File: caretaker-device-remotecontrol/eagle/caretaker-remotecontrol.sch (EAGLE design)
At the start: 50 parts, among them IC1 MAX1811N, IC2 ATMEGA168, IC3 XBee Series 2, IC4 ZLDO330, K1 BAT, K2 ISP, K3 USB-MINIB-5PIN, Q1 16MHz

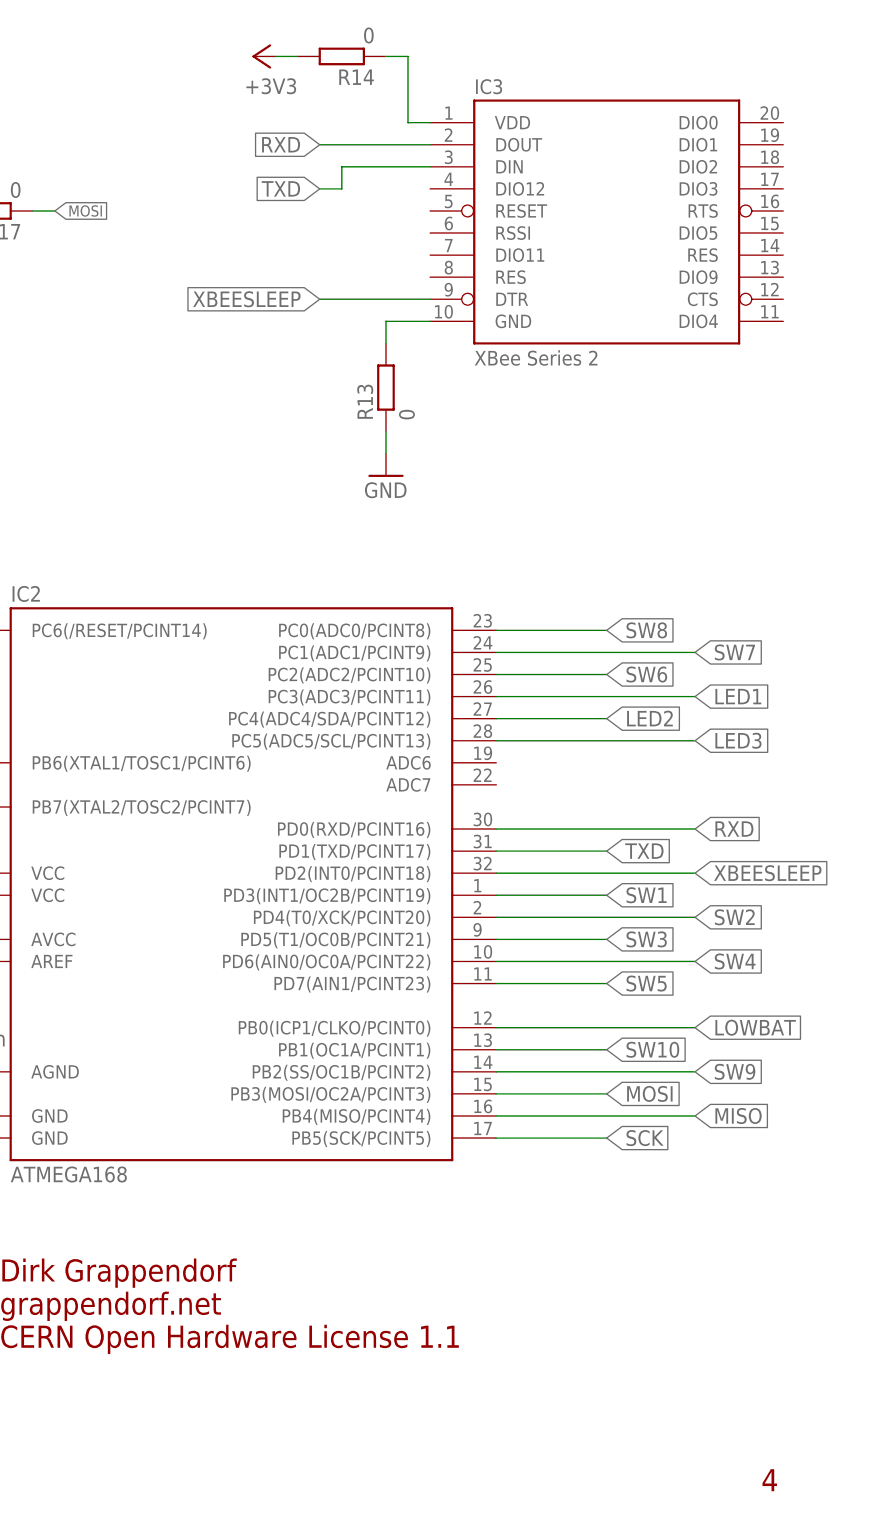
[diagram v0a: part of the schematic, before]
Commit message: feat: Convert the XBee RemoteControl device to a WLAN device
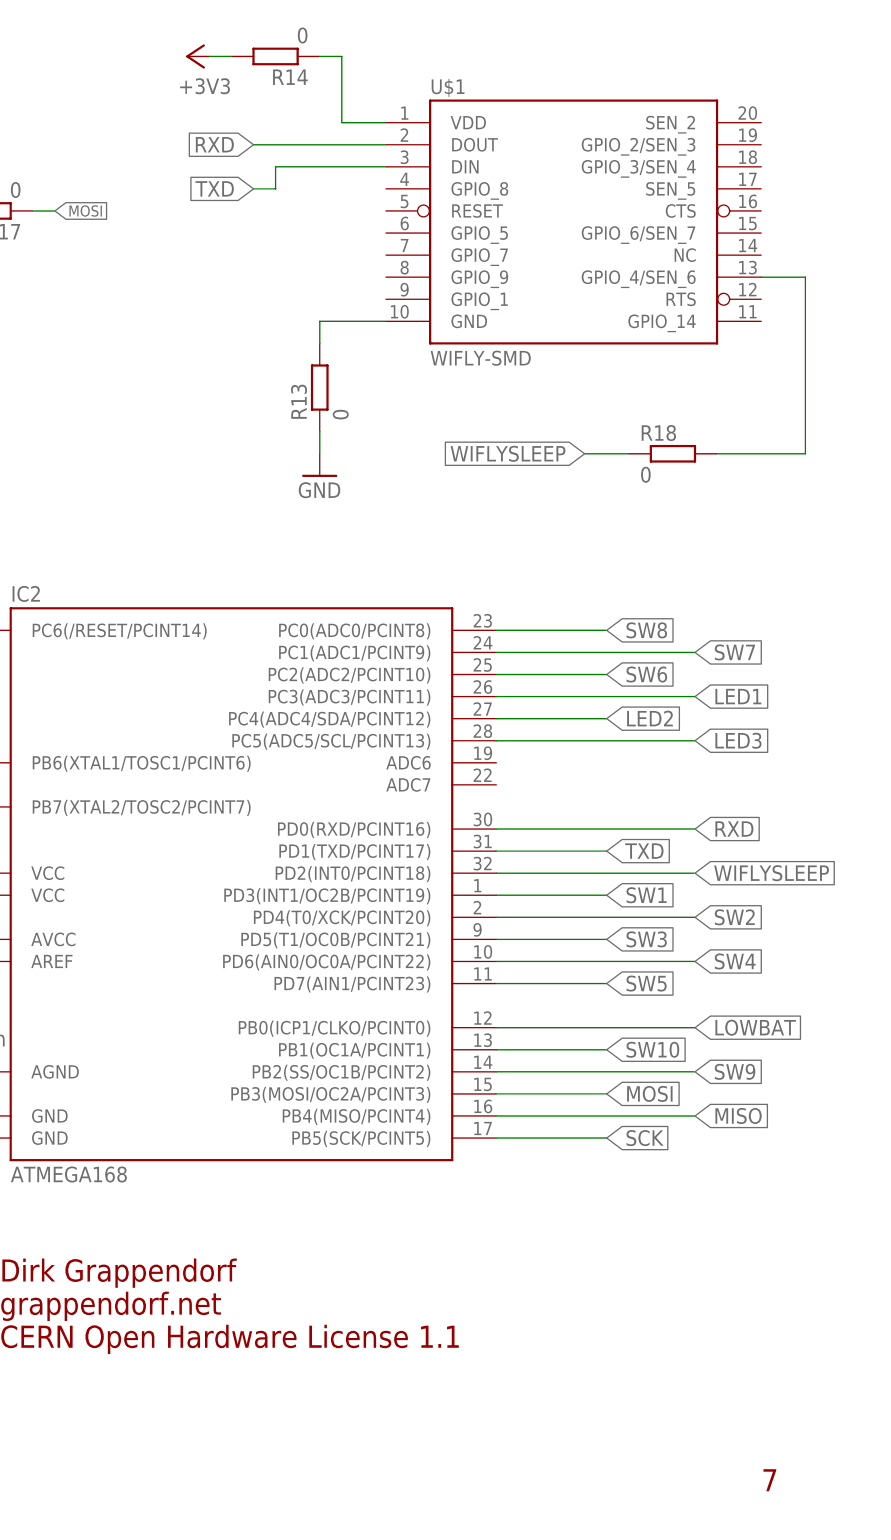
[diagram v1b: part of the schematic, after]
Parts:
- removed IC3: XBee Series 2, grapelabs:XBEE-1B4
- added R18: 0, rcl:R-EU_R1206
- added U$1: WIFLY-SMD, grapelabs:WIFLY-SMD
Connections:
- removed net XBEESLEEP: IC2.PD2(INT0/PCINT18), IC3.DTR
- new net N$27: R18.2, U$1.GPIO_4/SEN_6
- new net WIFLYSLEEP: IC2.PD2(INT0/PCINT18), R18.1
- net N$22: now also U$1.GND; no longer IC3.GND
- net N$23: now also U$1.VDD; no longer IC3.VDD
- net RXD: now also U$1.DOUT; no longer IC3.DOUT
- net TXD: now also U$1.DIN; no longer IC3.DIN
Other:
- note added: "7"
- note removed: "4"
- moved on the sheet: R13, R14
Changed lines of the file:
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@@
 <?xml version="1.0" encoding="utf-8"?>
 <!DOCTYPE eagle SYSTEM "eagle.dtd">
-<eagle version="6.4">
+<eagle version="6.5.0">
 <drawing>
 <settings>
@@
 <part name="GND4" library="supply1" deviceset="GND" device=""/>
 <part name="P+1" library="supply1" deviceset="+3V3" device=""/>
-<part name="IC3" library="grapelabs" deviceset="XBEE-1" device="B4" value="XBee Series 2"/>
 <part name="IC2" library="atmega8" deviceset="ATMEGA48/88/168" device="-AU" value="ATMEGA168"/>
 <part name="P+2" library="supply1" deviceset="+3V3" device=""/>
@@
 <part name="R16" library="rcl" deviceset="R-EU_" device="R1206" value="0"/>
 <part name="R17" library="rcl" deviceset="R-EU_" device="R1206" value="0"/>
+<part name="U$1" library="grapelabs" deviceset="WIFLY" device="-SMD"/>
+<part name="R18" library="rcl" deviceset="R-EU_" device="R1206" value="0"/>
 </parts>
 <sheets>
@@
 <plain>
 <text x="163.83" y="31.75" size="2.54" layer="94">Dirk Grappendorf</text>
-<text x="251.46" y="7.62" size="2.54" layer="94">4</text>
+<text x="251.46" y="7.62" size="2.54" layer="94">7</text>
 <text x="163.83" y="27.94" size="2.54" layer="94">grappendorf.net</text>
 <text x="163.83" y="24.13" size="2.54" layer="94">CERN Open Hardware License 1.1</text>
@@
 <instance part="GND4" gate="1" x="35.56" y="142.24"/>
 <instance part="P+1" gate="G$1" x="106.68" y="165.1" rot="R270"/>
-<instance part="IC3" gate="G$1" x="233.68" y="154.94"/>
 <instance part="IC2" gate="1" x="190.5" y="78.74"/>
-<instance part="P+2" gate="G$1" x="193.04" y="172.72" rot="R90"/>
-<instance part="GND1" gate="1" x="208.28" y="124.46"/>
+<instance part="P+2" gate="G$1" x="185.42" y="172.72" rot="R90"/>
+<instance part="GND1" gate="1" x="200.66" y="124.46"/>
 <instance part="GND2" gate="1" x="157.48" y="43.18"/>
 <instance part="P+3" gate="G$1" x="142.24" y="78.74" rot="R90"/>
@@
 <instance part="R11" gate="G$1" x="55.88" y="17.78"/>
 <instance part="R12" gate="G$1" x="68.58" y="17.78"/>
-<instance part="R13" gate="G$1" x="208.28" y="134.62" rot="R90"/>
-<instance part="R14" gate="G$1" x="203.2" y="172.72" rot="R180"/>
+<instance part="R13" gate="G$1" x="200.66" y="134.62" rot="R90"/>
+<instance part="R14" gate="G$1" x="195.58" y="172.72" rot="R180"/>
 <instance part="R15" gate="G$1" x="134.62" y="157.48" rot="R180"/>
 <instance part="R16" gate="G$1" x="134.62" y="154.94" rot="R180"/>
 <instance part="R17" gate="G$1" x="162.56" y="154.94" rot="R180"/>
+<instance part="U$1" gate="G$1" x="228.6" y="154.94"/>
+<instance part="R18" gate="G$1" x="241.3" y="127"/>
 </instances>
 <busses>
@@
 <pinref part="R14" gate="G$1" pin="2"/>
 <pinref part="P+2" gate="G$1" pin="+3V3"/>
-<wire x1="198.12" y1="172.72" x2="195.58" y2="172.72" width="0.1524" layer="91"/>
+<wire x1="190.5" y1="172.72" x2="187.96" y2="172.72" width="0.1524" layer="91"/>
 </segment>
 </net>
 <net name="TXD" class="0">
 <segment>
-<wire x1="213.36" y1="160.02" x2="203.2" y2="160.02" width="0.1524" layer="91"/>
-<wire x1="203.2" y1="160.02" x2="203.2" y2="157.48" width="0.1524" layer="91"/>
-<wire x1="203.2" y1="157.48" x2="200.66" y2="157.48" width="0.1524" layer="91"/>
-<label x="200.66" y="157.48" size="1.778" layer="95" rot="R180" xref="yes"/>
-<pinref part="IC3" gate="G$1" pin="DIN"/>
+<wire x1="208.28" y1="160.02" x2="195.58" y2="160.02" width="0.1524" layer="91"/>
+<wire x1="195.58" y1="160.02" x2="195.58" y2="157.48" width="0.1524" layer="91"/>
+<wire x1="195.58" y1="157.48" x2="193.04" y2="157.48" width="0.1524" layer="91"/>
+<label x="193.04" y="157.48" size="1.778" layer="95" rot="R180" xref="yes"/>
+<pinref part="U$1" gate="G$1" pin="DIN"/>
 </segment>
 <segment>
@@
 </segment>
 <segment>
-<wire x1="213.36" y1="162.56" x2="200.66" y2="162.56" width="0.1524" layer="91"/>
-<label x="200.66" y="162.56" size="1.778" layer="95" rot="R180" xref="yes"/>
-<pinref part="IC3" gate="G$1" pin="DOUT"/>
+<wire x1="208.28" y1="162.56" x2="193.04" y2="162.56" width="0.1524" layer="91"/>
+<label x="193.04" y="162.56" size="1.778" layer="95" rot="R180" xref="yes"/>
+<pinref part="U$1" gate="G$1" pin="DOUT"/>
 </segment>
 </net>
@@
 <pinref part="GND1" gate="1" pin="GND"/>
 <pinref part="R13" gate="G$1" pin="1"/>
-<wire x1="208.28" y1="127" x2="208.28" y2="129.54" width="0.1524" layer="91"/>
+<wire x1="200.66" y1="127" x2="200.66" y2="129.54" width="0.1524" layer="91"/>
 </segment>
 </net>
@@
 </segment>
 </net>
-<net name="XBEESLEEP" class="0">
-<segment>
-<wire x1="213.36" y1="144.78" x2="200.66" y2="144.78" width="0.1524" layer="91"/>
-<label x="200.66" y="144.78" size="1.778" layer="95" rot="R180" xref="yes"/>
-<pinref part="IC3" gate="G$1" pin="DTR"/>
-</segment>
+<net name="WIFLYSLEEP" class="0">
 <segment>
 <wire x1="220.98" y1="78.74" x2="243.84" y2="78.74" width="0.1524" layer="91"/>
 <label x="243.84" y="78.74" size="1.778" layer="95" xref="yes"/>
 <pinref part="IC2" gate="1" pin="PD2(INT0/PCINT18)"/>
+</segment>
+<segment>
+<pinref part="R18" gate="G$1" pin="1"/>
+<wire x1="236.22" y1="127" x2="231.14" y2="127" width="0.1524" layer="91"/>
+<label x="231.14" y="127" size="1.778" layer="95" rot="R180" xref="yes"/>
 </segment>
 </net>
@@
 <segment>
 <pinref part="R13" gate="G$1" pin="2"/>
-<wire x1="208.28" y1="139.7" x2="208.28" y2="142.24" width="0.1524" layer="91"/>
-<pinref part="IC3" gate="G$1" pin="GND"/>
-<wire x1="208.28" y1="142.24" x2="213.36" y2="142.24" width="0.1524" layer="91"/>
+<wire x1="200.66" y1="139.7" x2="200.66" y2="142.24" width="0.1524" layer="91"/>
+<wire x1="200.66" y1="142.24" x2="208.28" y2="142.24" width="0.1524" layer="91"/>
+<pinref part="U$1" gate="G$1" pin="GND"/>
 </segment>
 </net>
@@
 <segment>
 <pinref part="R14" gate="G$1" pin="1"/>
-<wire x1="208.28" y1="172.72" x2="210.82" y2="172.72" width="0.1524" layer="91"/>
-<wire x1="210.82" y1="172.72" x2="210.82" y2="165.1" width="0.1524" layer="91"/>
-<pinref part="IC3" gate="G$1" pin="VDD"/>
-<wire x1="210.82" y1="165.1" x2="213.36" y2="165.1" width="0.1524" layer="91"/>
+<wire x1="200.66" y1="172.72" x2="203.2" y2="172.72" width="0.1524" layer="91"/>
+<wire x1="203.2" y1="172.72" x2="203.2" y2="165.1" width="0.1524" layer="91"/>
+<wire x1="203.2" y1="165.1" x2="208.28" y2="165.1" width="0.1524" layer="91"/>
+<pinref part="U$1" gate="G$1" pin="VDD"/>
 </segment>
 </net>
@@
 </segment>
 </net>
+<net name="N$27" class="0">
+<segment>
+<pinref part="U$1" gate="G$1" pin="GPIO_4/SEN_6"/>
+<wire x1="251.46" y1="147.32" x2="256.54" y2="147.32" width="0.1524" layer="91"/>
+<wire x1="256.54" y1="147.32" x2="256.54" y2="127" width="0.1524" layer="91"/>
+<pinref part="R18" gate="G$1" pin="2"/>
+<wire x1="256.54" y1="127" x2="246.38" y2="127" width="0.1524" layer="91"/>
+</segment>
+</net>
